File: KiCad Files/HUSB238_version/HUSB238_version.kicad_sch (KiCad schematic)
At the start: 20 parts, among them J9 USB_C_Receptacle_USB2.0_14P, Q2 AONR21307, U3 HUSB238_USB_PD, U4 USBLC6-2SC6, U5 LM393

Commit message: changed pcb
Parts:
- removed D1: 6.2V SMD Zener, Diode_SMD:D_0805_2012Metric_Pad1.15x1.40mm_HandSolder, symbol Device:D_Zener_Small
- removed R19: 15k, Resistor_SMD:R_0805_2012Metric_Pad1.20x1.40mm_HandSolder, symbol PCM_SL_Resistors:4.7k
- removed R20: 10k, Resistor_SMD:R_0805_2012Metric_Pad1.20x1.40mm_HandSolder, symbol PCM_SL_Resistors:4.7k
- removed R21: 1.2k Ohm, Resistor_SMD:R_0805_2012Metric_Pad1.20x1.40mm_HandSolder, symbol PCM_SL_Resistors:1k
- removed U5: LM393, Package_SO:SOIC-8_5.3x6.2mm_P1.27mm, symbol Comparator:LM393
- added J2, J3: Conn_02x02_Counter_Clockwise, Connector_PinHeader_2.54mm:PinHeader_2x03_P2.54mm_Vertical_SMD, symbol Connector_Generic:Conn_02x03_Odd_Even
- added Q9: AO3400A, Package_TO_SOT_SMD:SOT-23, symbol Transistor_FET:AO3400A
- added R16: 6.04k, Resistor_SMD:R_0805_2012Metric_Pad1.20x1.40mm_HandSolder, symbol PCM_SL_Resistors:4.7k
- added R22: 150 Ohm, Resistor_SMD:R_0805_2012Metric_Pad1.20x1.40mm_HandSolder, symbol PCM_SL_Resistors:1k
- added SW1: SW_DIP_x05, symbol Switch:SW_DIP_x05
- R17: value 4.7k -> 14k
- R18: value 10k -> 7.8k
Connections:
- net GND: now also R17.1, R18.1, J2.1 (Pin_1), J2.3 (Pin_3), J2.5 (Pin_5), J3.1 (Pin_1), J3.3 (Pin_3), J3.5 (Pin_5), Q9.2 (S), R16.1, SW1.10
- net at J9.A4 (VBUS), J9.A9 (VBUS), J9.B4 (VBUS)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: now also D7.2 (A); no longer R17.1, R18.2
- net at Q2.4, R13.2, R14.1: now also Q9.1 (G)
- net VCC: now reaches C4.2, C5.2, C6.2, Q2.5_6_7_8
- net VCC: now also J2.2 (Pin_2), J2.4 (Pin_4), J2.6 (Pin_6), J3.2 (Pin_2), J3.4 (Pin_4), J3.6 (Pin_6)
- net at R17.2: now also SW1.7
- net at U3.8 (VSET): now also SW1.1, SW1.2, SW1.3, SW1.4, SW1.5; no longer R15.2
- net at D7.1 (K): now also R22.1
- new net: R18.2, SW1.6
- new net: R16.2, SW1.9
- new net: R15.2, SW1.8
- new net: Q9.3 (D), R22.2
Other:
- moved on the sheet: D7, R15

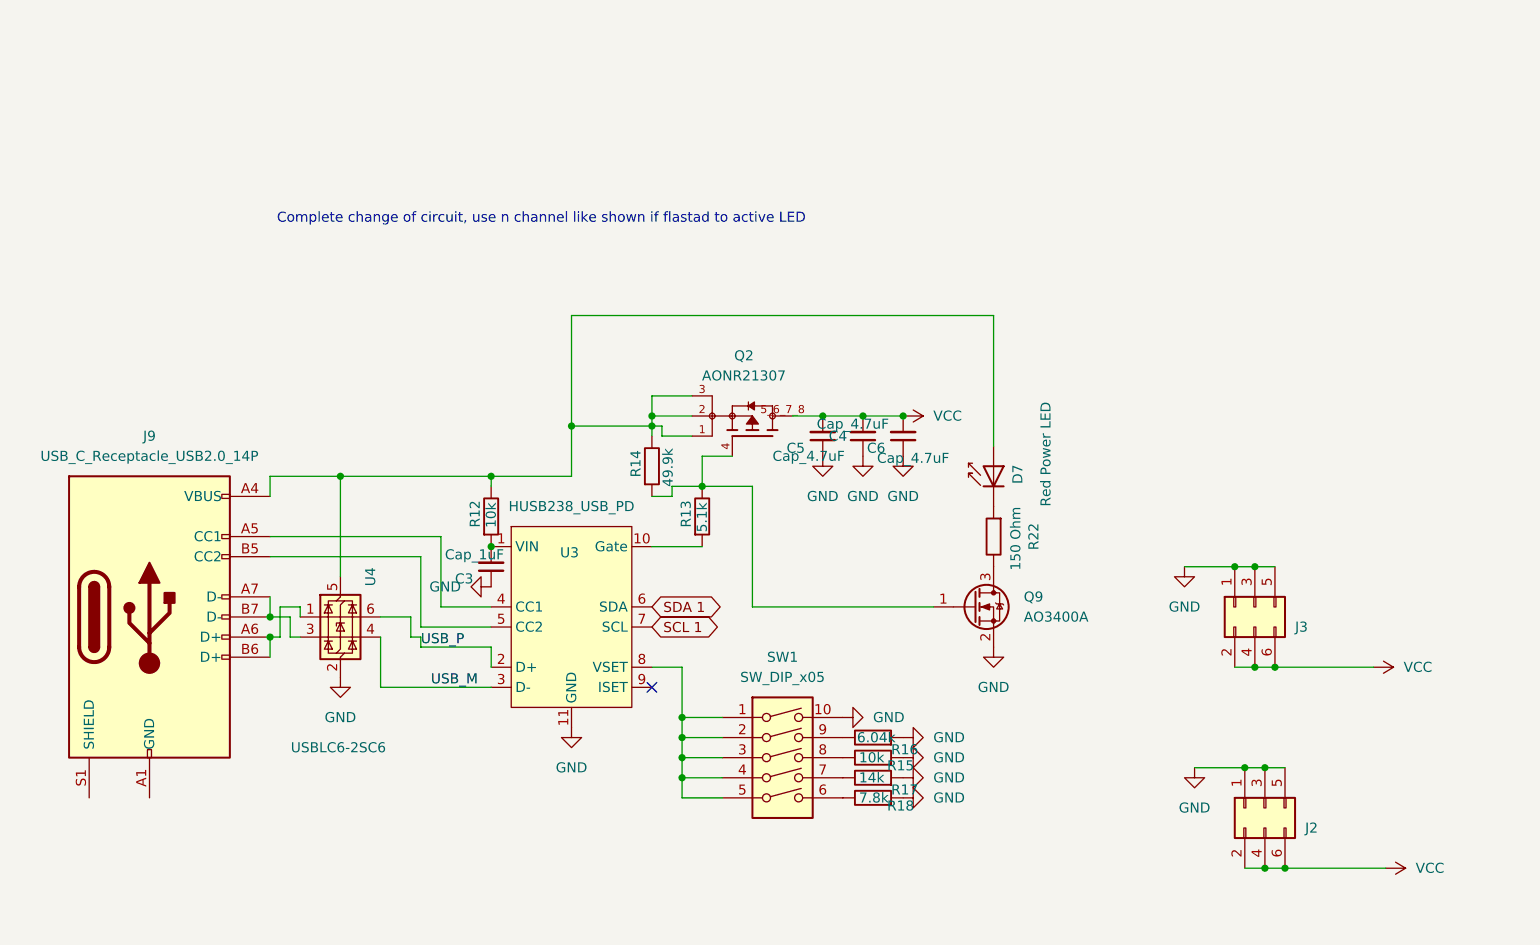
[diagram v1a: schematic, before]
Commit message: almost finished husb238 version
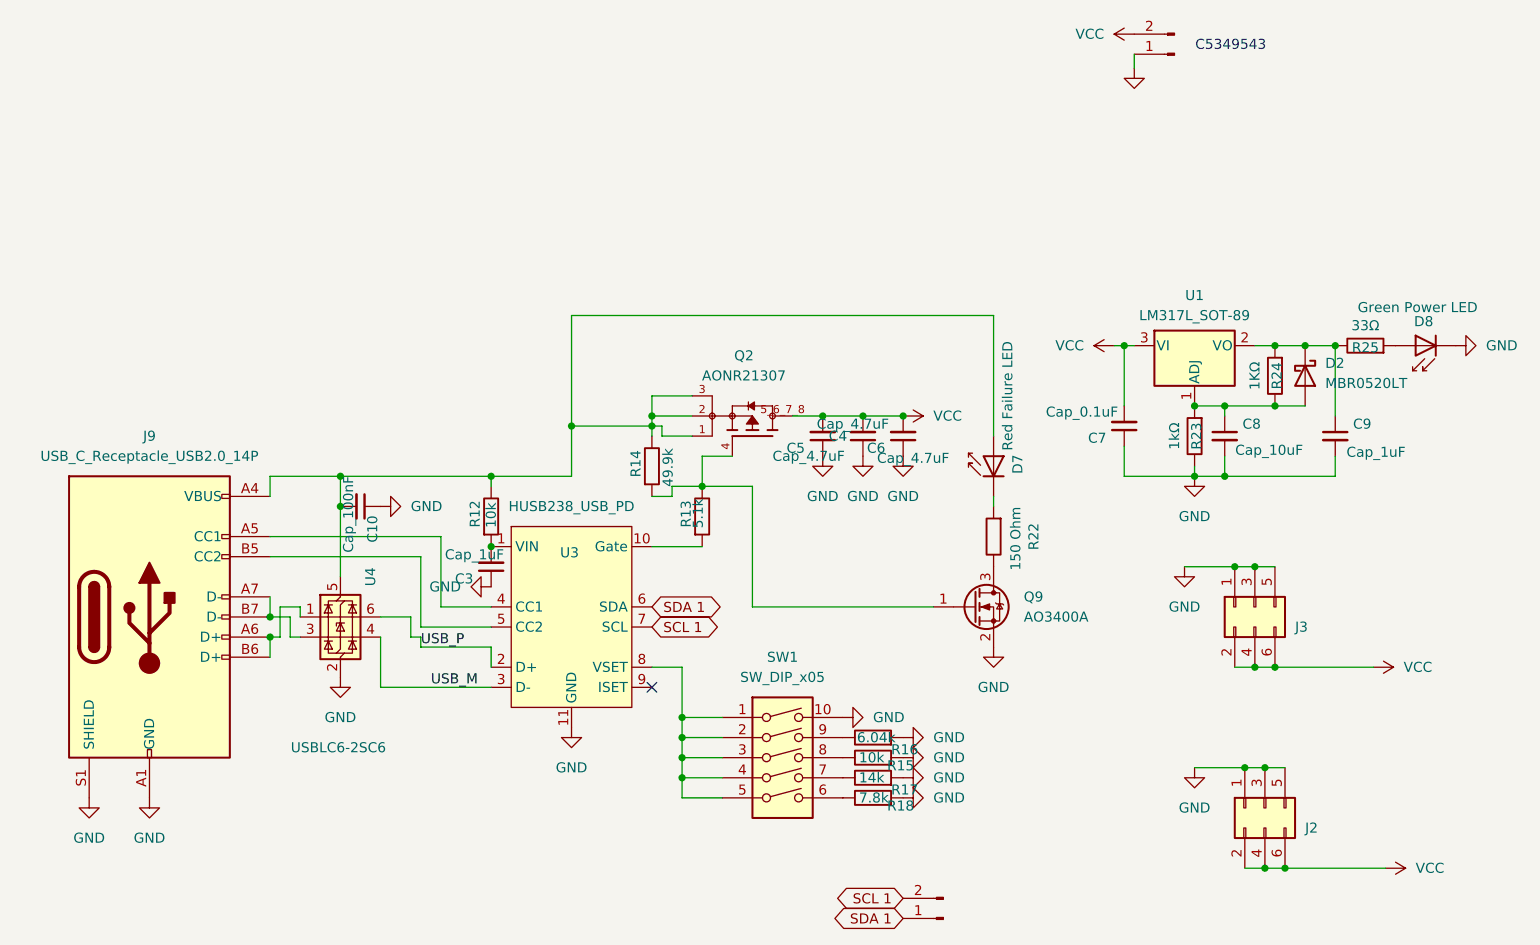
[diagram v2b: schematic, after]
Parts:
- added C10: Cap_100nF, Capacitor_SMD:C_0402_1005Metric_Pad0.74x0.62mm_HandSolder, symbol Device:C_Small
- added C7: Cap_0.1uF, Capacitor_SMD:C_0402_1005Metric_Pad0.74x0.62mm_HandSolder, symbol Device:C_Small
- added C8: Cap_10uF, Capacitor_SMD:C_0402_1005Metric_Pad0.74x0.62mm_HandSolder, symbol Device:C_Small
- added C9: Cap_1uF, Capacitor_SMD:C_0402_1005Metric_Pad0.74x0.62mm_HandSolder, symbol Device:C_Small
- added D2: MBR0520LT, Diode_SMD:D_SOD-123, symbol Diode:MBR0520LT
- added D8: Green Power LED, LED_SMD:LED_0603_1608Metric_Pad1.05x0.95mm_HandSolder, symbol Custom_Parts:LED
- added J4: Conn_01x02_Pin, TerminalBlock_TE-Connectivity:TerminalBlock_TE_282834-2_1x02_P2.54mm_Horizontal, symbol Connector:Conn_01x02_Pin
- added N21: Conn_01x02_Pin, Connector_PinHeader_2.54mm:PinHeader_1x02_P2.54mm_Vertical, symbol Connector:Conn_01x02_Pin
- added R23: 1kΩ, Resistor_SMD:R_0402_1005Metric_Pad0.72x0.64mm_HandSolder, symbol PCM_SL_Resistors:1k
- added R24: 1KΩ, Resistor_SMD:R_0402_1005Metric_Pad0.72x0.64mm_HandSolder, symbol PCM_SL_Resistors:1k
- added R25: 33Ω, Resistor_SMD:R_0402_1005Metric_Pad0.72x0.64mm_HandSolder, symbol PCM_SL_Resistors:1k
- added U1: LM317L_SOT-89, Package_TO_SOT_SMD:SOT-89-3, symbol Regulator_Linear:LM317L_SOT-89
- C3, C4, C5, C6: footprint Capacitor_SMD:C_0805_2012Metric_Pad1.18x1.45mm_HandSolder -> Capacitor_SMD:C_0402_1005Metric_Pad0.74x0.62mm_HandSolder
- D7: value Red Power LED -> Red Failure LED; footprint LED_SMD:LED_0805_2012Metric_Pad1.15x1.40mm_HandSolder -> LED_SMD:LED_0603_1608Metric_Pad1.05x0.95mm_HandSolder
- Q2: footprint mosfet:TRANS_AONR21307 -> AONR21307:TRANS_AONR21307
- R12, R13, R14, R15, R16, R17, R18, R22: footprint Resistor_SMD:R_0805_2012Metric_Pad1.20x1.40mm_HandSolder -> Resistor_SMD:R_0402_1005Metric_Pad0.72x0.64mm_HandSolder
- SW1: footprint (none) -> Button_Switch_SMD:SW_DIP_SPSTx05_Slide_6.7x14.26mm_W8.61mm_P2.54mm_LowProfile
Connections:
- net GND: now also J9.A1 (GND), J9.A12 (GND), J9.B1 (GND), J9.B12 (GND), J9.S1 (SHIELD), C10.1, C7.1, C8.2, C9.2, D8.1 (K), J4.1 (Pin_1), R23.2
- net SCL 1: now also N21.2 (Pin_2)
- net SDA 1: now also N21.1 (Pin_1)
- net VCC: now also C7.2, J4.2 (Pin_2), U1.3 (VI)
- net at D7.2 (A), J9.A4 (VBUS), J9.A9 (VBUS)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: now also C10.2
- new net: D8.2 (A), R25.1
- new net: C9.1, D2.1 (K), R24.1, R25.2, U1.2 (VO)
- new net: C8.1, D2.2 (A), R23.1, R24.2, U1.1 (ADJ)
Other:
- note added: "C5349543"
- note removed: "Complete change of circuit, use n channel like shown if flastad to active LED"
- moved on the sheet: D7

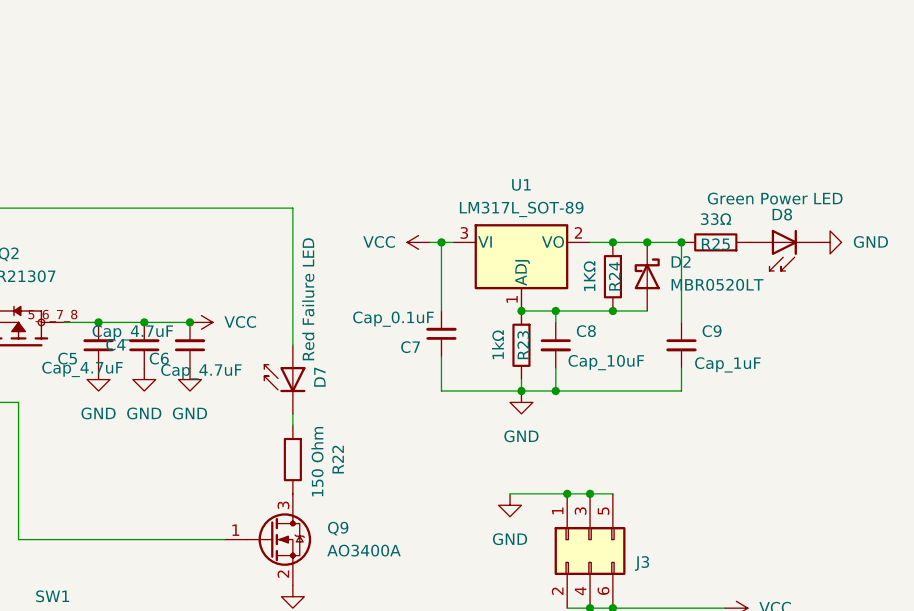
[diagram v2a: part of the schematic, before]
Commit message: many changes and new pcb design. Also updated husb238 design after boards arraived
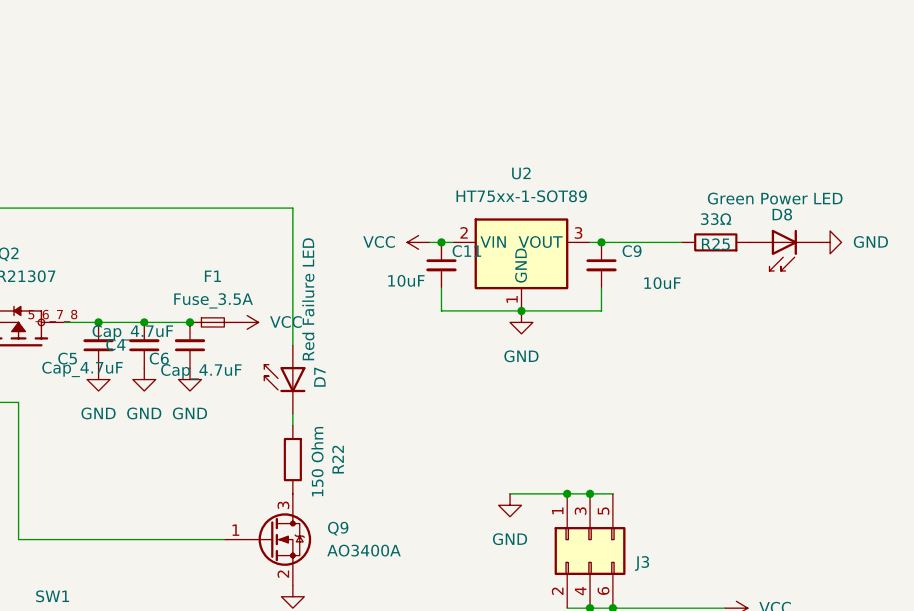
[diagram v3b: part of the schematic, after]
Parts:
- removed C7: Cap_0.1uF, Capacitor_SMD:C_0402_1005Metric_Pad0.74x0.62mm_HandSolder, symbol Device:C_Small
- removed C8: Cap_10uF, Capacitor_SMD:C_0402_1005Metric_Pad0.74x0.62mm_HandSolder, symbol Device:C_Small
- removed D2: MBR0520LT, Diode_SMD:D_SOD-123, symbol Diode:MBR0520LT
- removed R23: 1kΩ, Resistor_SMD:R_0402_1005Metric_Pad0.72x0.64mm_HandSolder, symbol PCM_SL_Resistors:1k
- removed R24: 1KΩ, Resistor_SMD:R_0402_1005Metric_Pad0.72x0.64mm_HandSolder, symbol PCM_SL_Resistors:1k
- removed U1: LM317L_SOT-89, Package_TO_SOT_SMD:SOT-89-3, symbol Regulator_Linear:LM317L_SOT-89
- added C11: 10uF, Capacitor_SMD:C_0402_1005Metric_Pad0.74x0.62mm_HandSolder, symbol Device:C_Small
- added F1: Fuse_3.5A, Capacitor_SMD:C_1808_4520Metric_Pad1.72x2.30mm_HandSolder, symbol Device:Fuse_Small
- added U2: HT75xx-1-SOT89, Package_TO_SOT_SMD:SOT-89-3, symbol Regulator_Linear:HT75xx-1-SOT89
- C9: value Cap_1uF -> 10uF
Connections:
- net GND: now also C11.2, U2.1 (GND)
- net VCC: now also C11.1, F1.2, U2.2 (VIN); no longer C4.2, C5.2, C6.2, Q2.5_6_7_8
- net at C9.1, R25.2: now also U2.3 (VOUT)
- new net: C4.2, C5.2, C6.2, F1.1, Q2.5_6_7_8
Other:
- moved on the sheet: C9
